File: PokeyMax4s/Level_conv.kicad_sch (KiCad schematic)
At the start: 3 parts, among them U2 74CB3T16210, U4 74CB3T16210

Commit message: PokeyMax 4s fabrication files
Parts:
- U2: JLCPCB Rotation Offset 90 -> 270
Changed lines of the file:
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@@
 			)
 		)
-		(property "JLCPCB Rotation Offset" "90"
+		(property "JLCPCB Rotation Offset" "270"
 			(at 166.37 82.55 0)
 			(effects

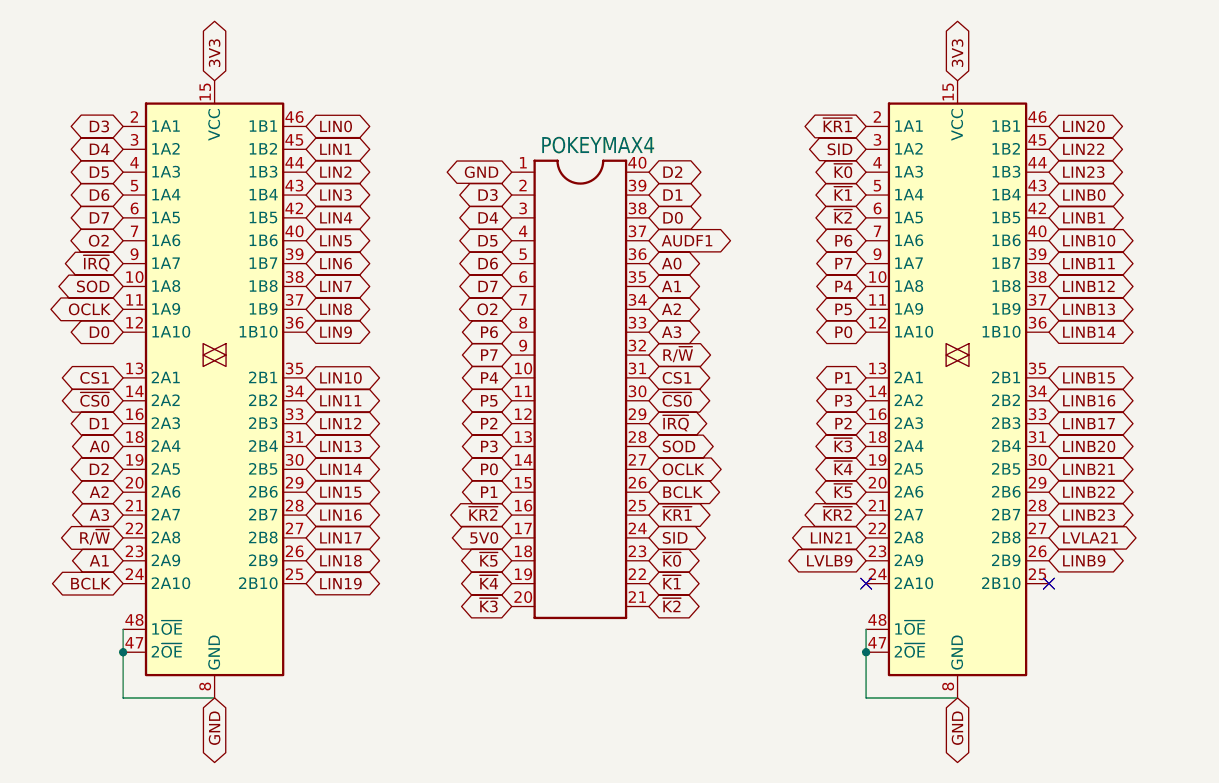
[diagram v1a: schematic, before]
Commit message: Add A4 to PokeyMax 4s
Reroute accordingly
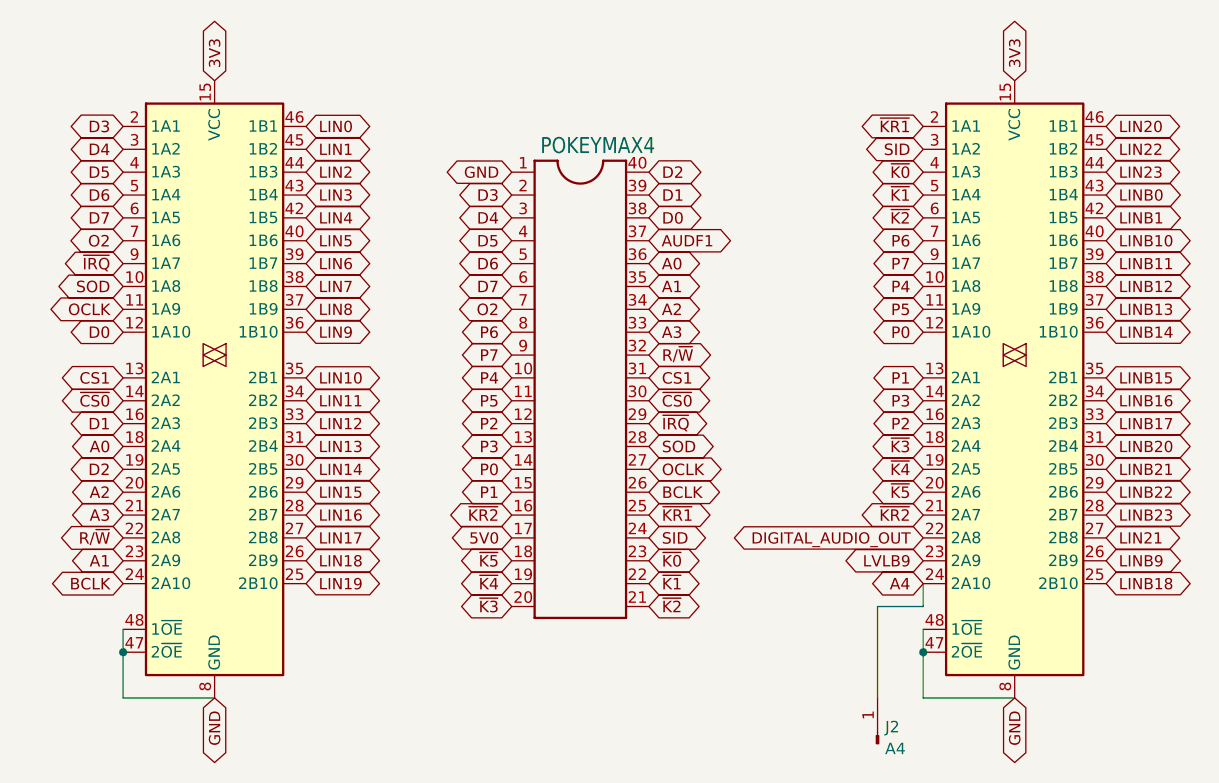
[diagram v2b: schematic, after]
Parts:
- added J2: A4, Connector_PinHeader_2.54mm:PinHeader_1x01_P2.54mm_Vertical, symbol Connector:Conn_01x01_Pin
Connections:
- net LVLA21 is gone; now on net LIN21: U2.27 (2B8)
- net LIN21: no longer U2.22 (2A8)
- net A4: now reaches U2.24 (2A10)
- net A4: now also J2.1 (Pin_1)
- net LINB18: now reaches U2.25 (2B10)
- new net DIGITAL_AUDIO_OUT: U2.22 (2A8)
- no-connect marks 2 -> 0

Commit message: Fix LIN22 to AUD1 erroneous connection
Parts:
- U2, U4: LCSC Part # C2674762 -> C2674635
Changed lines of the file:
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@@
 (kicad_sch
-	(version 20231120)
+	(version 20250114)
 	(generator "eeschema")
-	(generator_version "8.0")
+	(generator_version "9.0")
 	(paper "A4")
 	(junction
@@
 			)
 		)
-		(property "LCSC Part #" "C2674762"
+		(property "LCSC Part #" "C2674635"
 			(at 172.72 82.55 0)
 			(effects
@@
 			)
 		)
-		(property "LCSC Part #" "C2674762"
+		(property "LCSC Part #" "C2674635"
 			(at 83.82 82.55 0)
 			(effects
